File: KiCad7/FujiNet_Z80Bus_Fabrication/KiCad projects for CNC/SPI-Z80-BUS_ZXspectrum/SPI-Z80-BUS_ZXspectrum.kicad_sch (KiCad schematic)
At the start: 13 parts

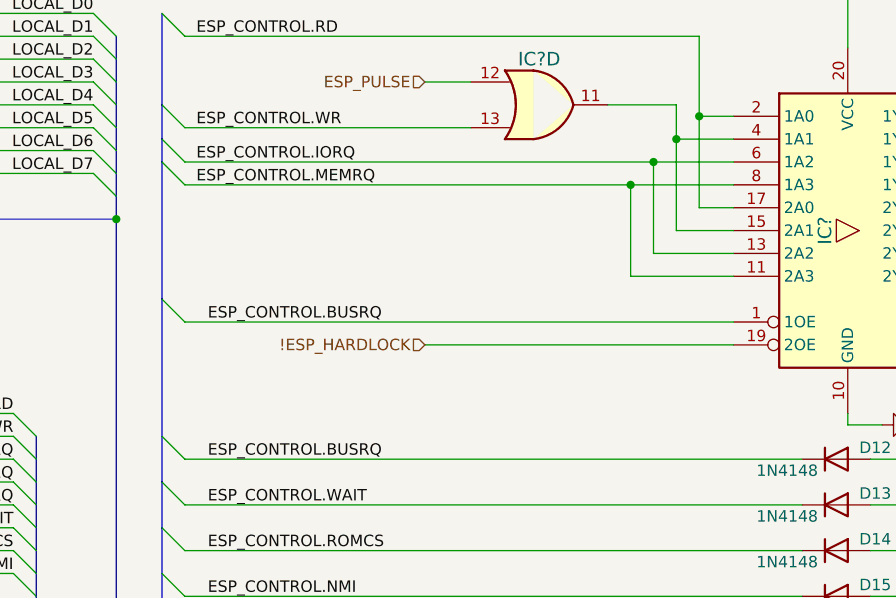
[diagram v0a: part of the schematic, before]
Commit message: KiCad SPI fixed
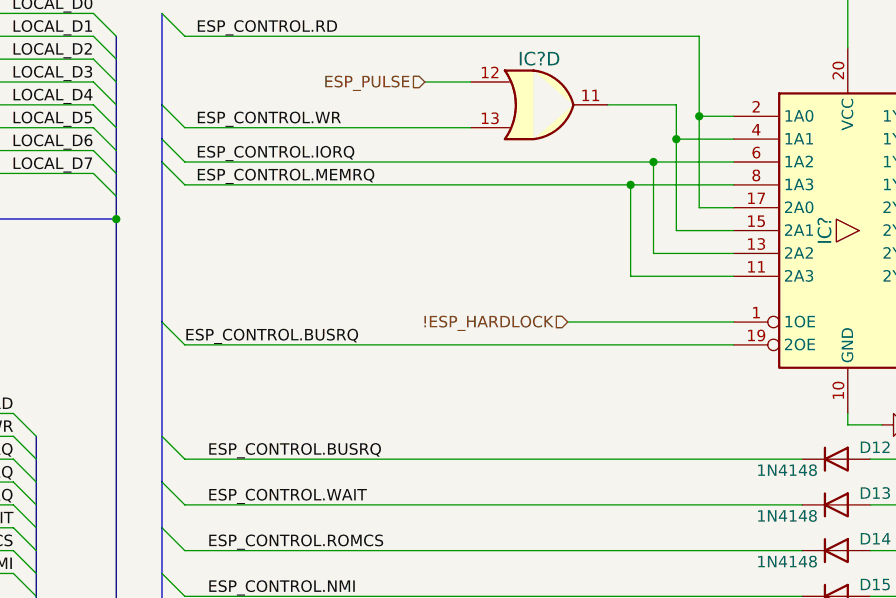
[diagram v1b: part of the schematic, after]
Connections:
- net !ESP_HARDLOCK: now also IC?.1 (1OE); no longer IC?.19 (2OE)
- net ESP_CONTROL.BUSRQ: now also IC?.19 (2OE); no longer IC?.1 (1OE)
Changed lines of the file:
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@@
     (comment 2 "SPI Bus to couple the ESP32 to the Local Bus and Z80 Bus")
   )
+  (bus_alias "ESP_CONTROL" (members "ESP_CONTROL.RD" "ESP_CONTROL.WR" "ESP_CONTROL.IORQ" "ESP_CONTROL.MEMRQ" "ESP_CONTROL.BUSRQ" "ESP_CONTROL.WAIT" "ESP_CONTROL.ROMCS" "ESP_CONTROL.NMI"))
+  (bus_alias "LOCAL_CONTROL" (members "LOCAL_CONTROL.RD" "LOCAL_CONTROL.WR" "LOCAL_CONTROL.IORQ" "LOCAL_CONTROL.MEMRQ"))
   (bus_alias "ESP_SPI_INTERNAL" (members "ESP_SPI_INT.MOSI" "ESP_SPI_INT.SCK" "ESP_SPI_INT.MR" "ESP_SPI_INT.STC" "ESP_SPI_INT.CE" "ESP_SPI_INT.PL" "ESP_SPI_INT.MISO" "ESP_SPI_INT.OE" ""))
-  (bus_alias "LOCAL_CONTROL" (members "LOCAL_CONTROL.RD" "LOCAL_CONTROL.WR" "LOCAL_CONTROL.IORQ" "LOCAL_CONTROL.MEMRQ"))
-  (bus_alias "ESP_CONTROL" (members "ESP_CONTROL.RD" "ESP_CONTROL.WR" "ESP_CONTROL.IORQ" "ESP_CONTROL.MEMRQ" "ESP_CONTROL.BUSRQ" "ESP_CONTROL.WAIT" "ESP_CONTROL.ROMCS" "ESP_CONTROL.NMI"))
   (junction (at 99.06 55.88) (diameter 0) (color 0 0 0 0)
   )
@@
     (stroke (width 0) (type default))
   )
-  (bus_entry (at 142.24 87.63) (size 2.54 2.54)
+  (bus_entry (at 142.24 90.17) (size 2.54 2.54)
     (stroke (width 0) (type default))
   )
@@
     (stroke (width 0) (type default))
   )
-  (wire (pts (xy 144.78 90.17) (xy 205.74 90.17))
-    (stroke (width 0) (type default))
-  )
   (wire (pts (xy 199.39 80.01) (xy 199.39 69.85))
     (stroke (width 0) (type default))
@@
     (stroke (width 0) (type default))
   )
+  (wire (pts (xy 144.78 92.71) (xy 205.74 92.71))
+    (stroke (width 0) (type default))
+  )
   (wire (pts (xy 101.6 58.42) (xy 101.6 54.61))
     (stroke (width 0) (type default))
@@
     (stroke (width 0) (type default))
   )
+  (bus (pts (xy 142.24 90.17) (xy 142.24 102.87))
+    (stroke (width 0) (type default))
+  )
   (wire (pts (xy 196.85 72.39) (xy 144.78 72.39))
     (stroke (width 0) (type default))
@@
     (stroke (width 0) (type default))
   )
-  (bus (pts (xy 142.24 87.63) (xy 142.24 102.87))
-    (stroke (width 0) (type default))
-  )
   (wire (pts (xy 232.41 43.18) (xy 232.41 46.99))
     (stroke (width 0) (type default))
@@
     (stroke (width 0) (type default))
   )
-  (bus (pts (xy 142.24 72.39) (xy 142.24 87.63))
+  (bus (pts (xy 142.24 72.39) (xy 142.24 90.17))
     (stroke (width 0) (type default))
   )
@@
     (stroke (width 0) (type default))
   )
-  (wire (pts (xy 171.45 92.71) (xy 205.74 92.71))
-    (stroke (width 0) (type default))
-  )
   (wire (pts (xy 134.62 71.12) (xy 114.3 71.12))
     (stroke (width 0) (type default))
@@
     (stroke (width 0) (type default))
   )
+  (wire (pts (xy 187.325 90.17) (xy 205.74 90.17))
+    (stroke (width 0) (type default))
+  )
   (wire (pts (xy 41.91 39.37) (xy 62.23 39.37))
     (stroke (width 0) (type default))
@@
     (effects (font (size 1.27 1.27)) (justify right bottom))
   )
-  (label "ESP_CONTROL.BUSRQ" (at 147.32 90.17 0) (fields_autoplaced)
+  (label "ESP_CONTROL.BUSRQ" (at 144.78 92.71 0) (fields_autoplaced)
     (effects (font (size 1.27 1.27)) (justify left bottom))
   )
@@
     (effects (font (size 1.27 1.27)) (justify right))
   )
-  (hierarchical_label "!ESP_HARDLOCK" (shape input) (at 171.45 92.71 180) (fields_autoplaced)
+  (hierarchical_label "!ESP_HARDLOCK" (shape input) (at 187.325 90.17 180) (fields_autoplaced)
     (effects (font (size 1.27 1.27)) (justify right))
   )
